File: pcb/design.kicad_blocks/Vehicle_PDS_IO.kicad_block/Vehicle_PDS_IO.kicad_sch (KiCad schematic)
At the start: 1 part, among them J4 FFC2B28-24-G

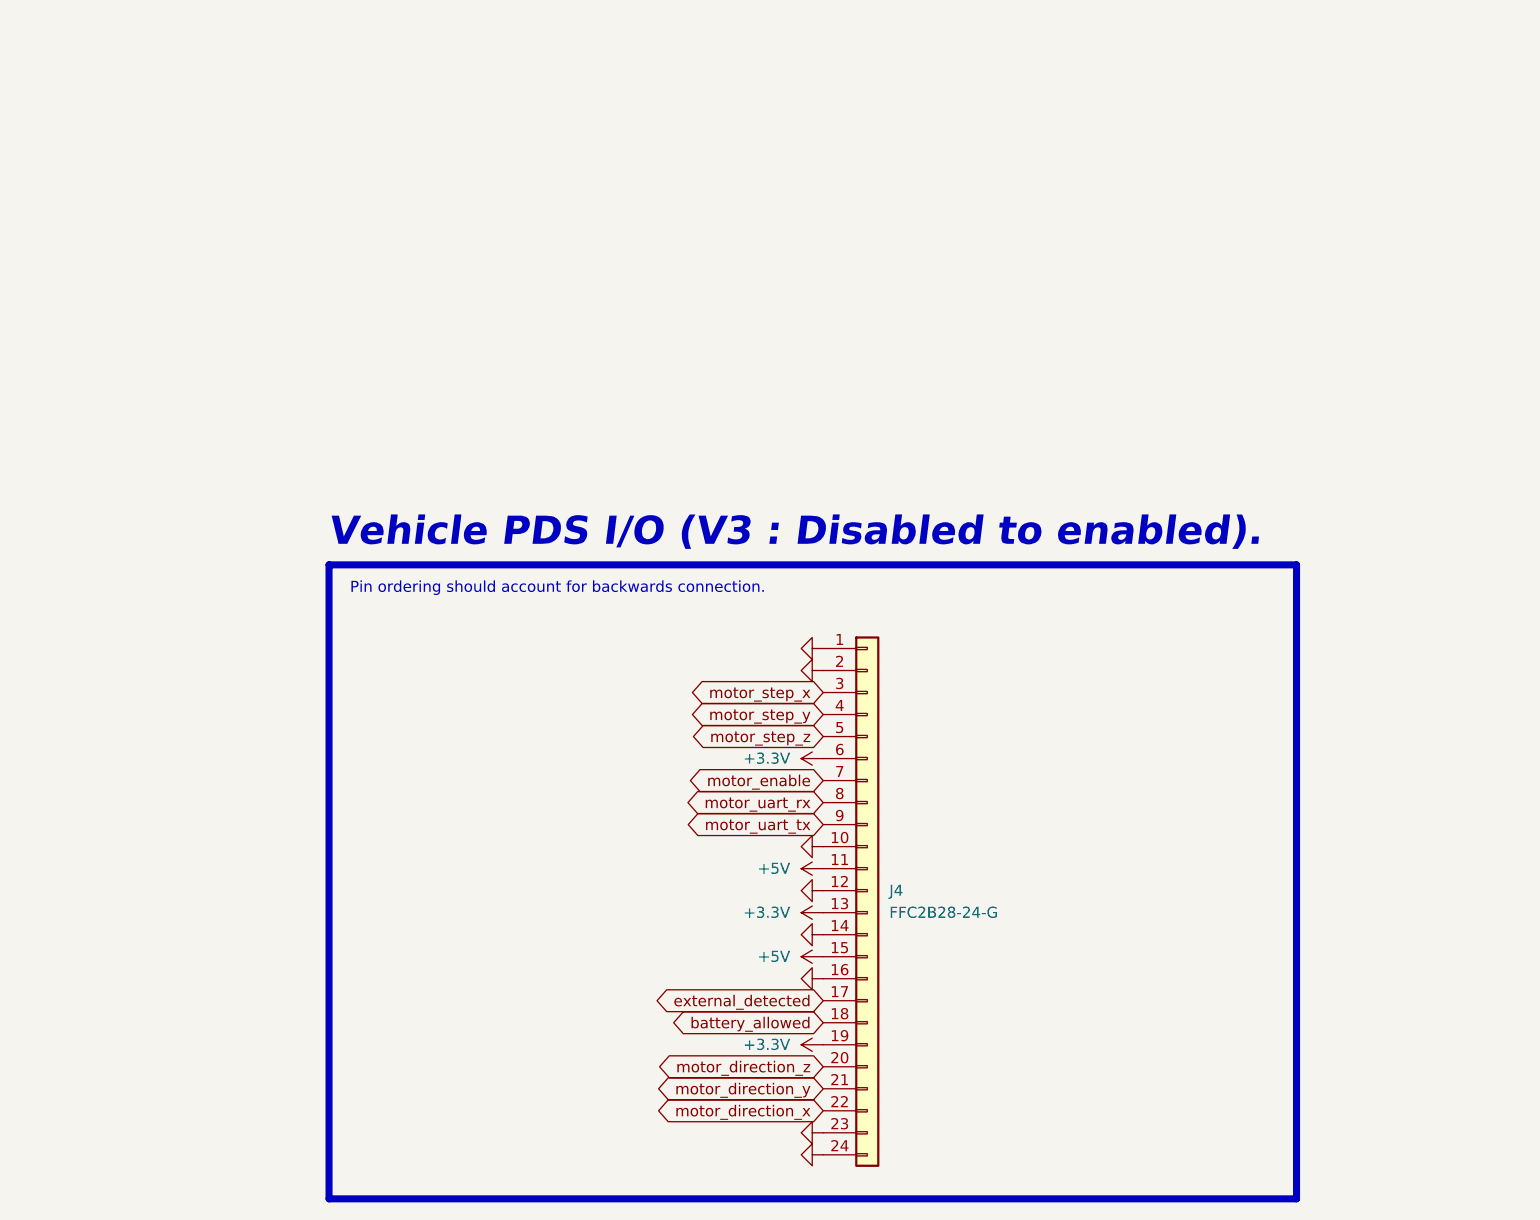
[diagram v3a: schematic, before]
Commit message: Addressed ERC schematic issues for `VehicleFlightComputer`.
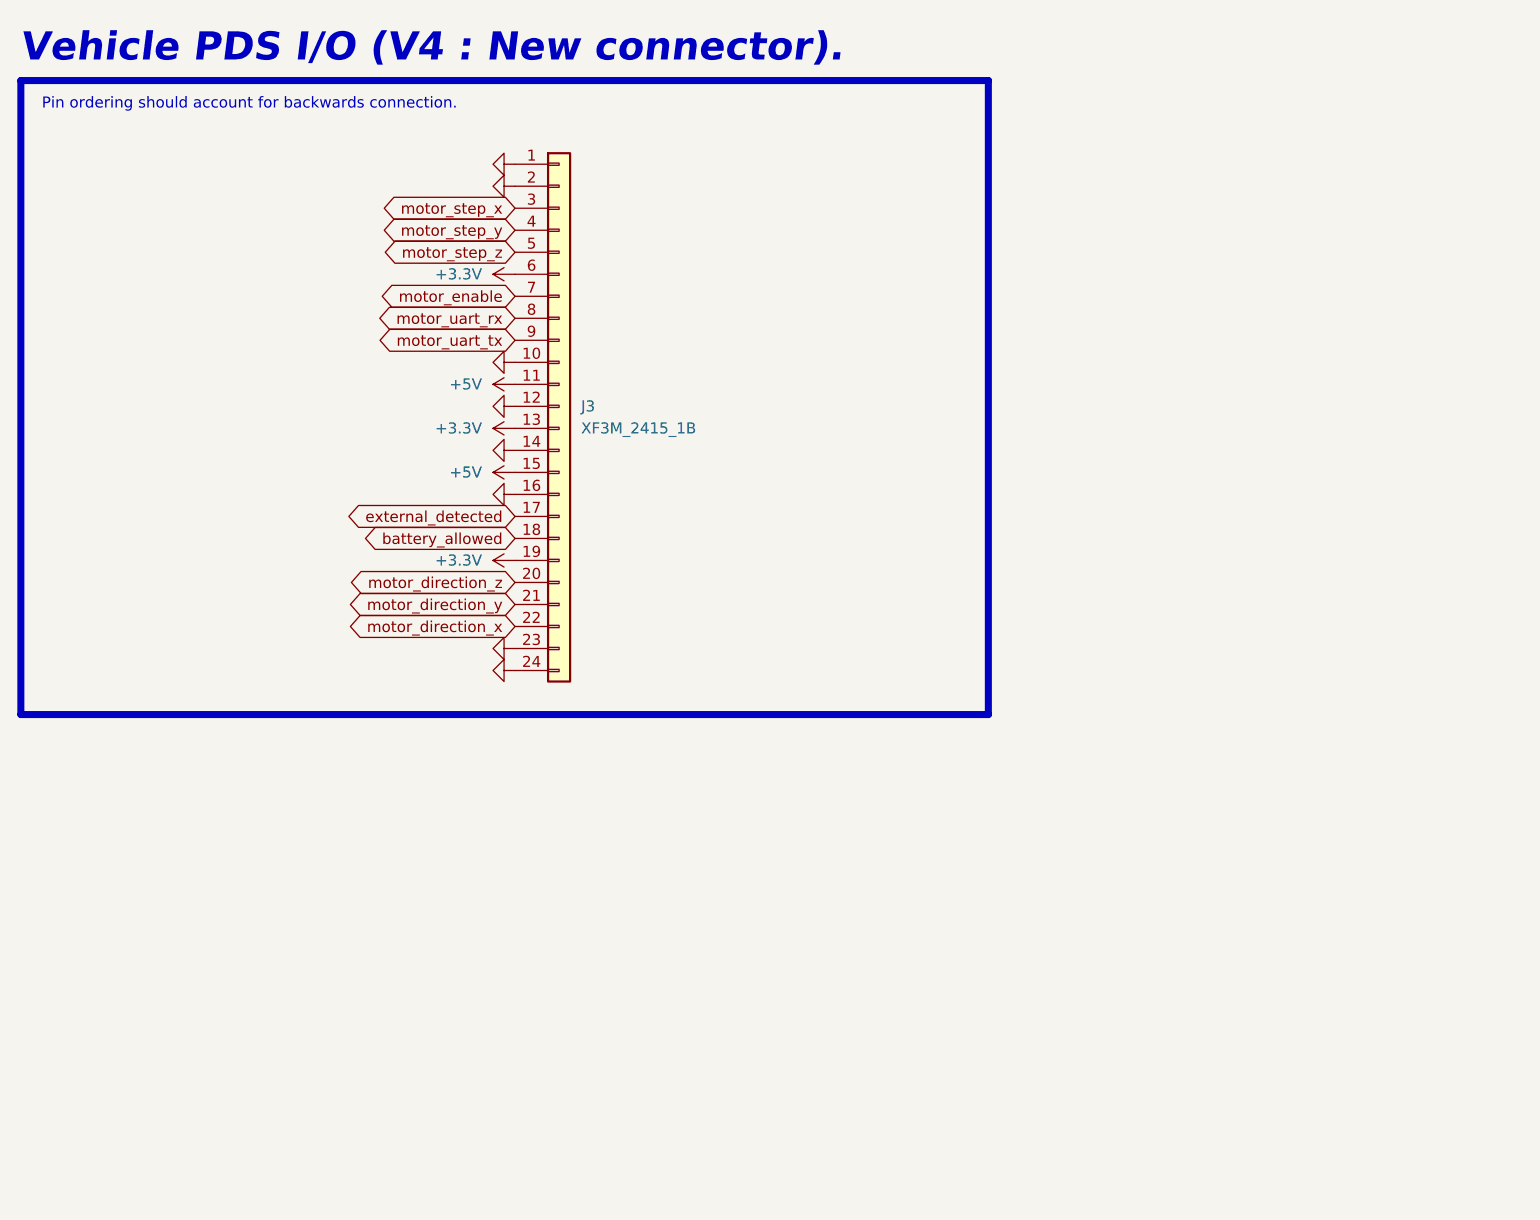
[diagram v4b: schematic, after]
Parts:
- J3: renamed from J4; value FFC2B28-24-G -> XF3M_2415_1B; footprint pcb:Flat Flexible Cable 24-Pin 0.5mm Connector -> pcb:XF3M_2415_1B
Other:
- note added: "Vehicle PDS I/O (V4 : New connector)."
- note removed: "Vehicle PDS I/O (V3 : Disabled to enabled)."
- moved on the sheet: J3

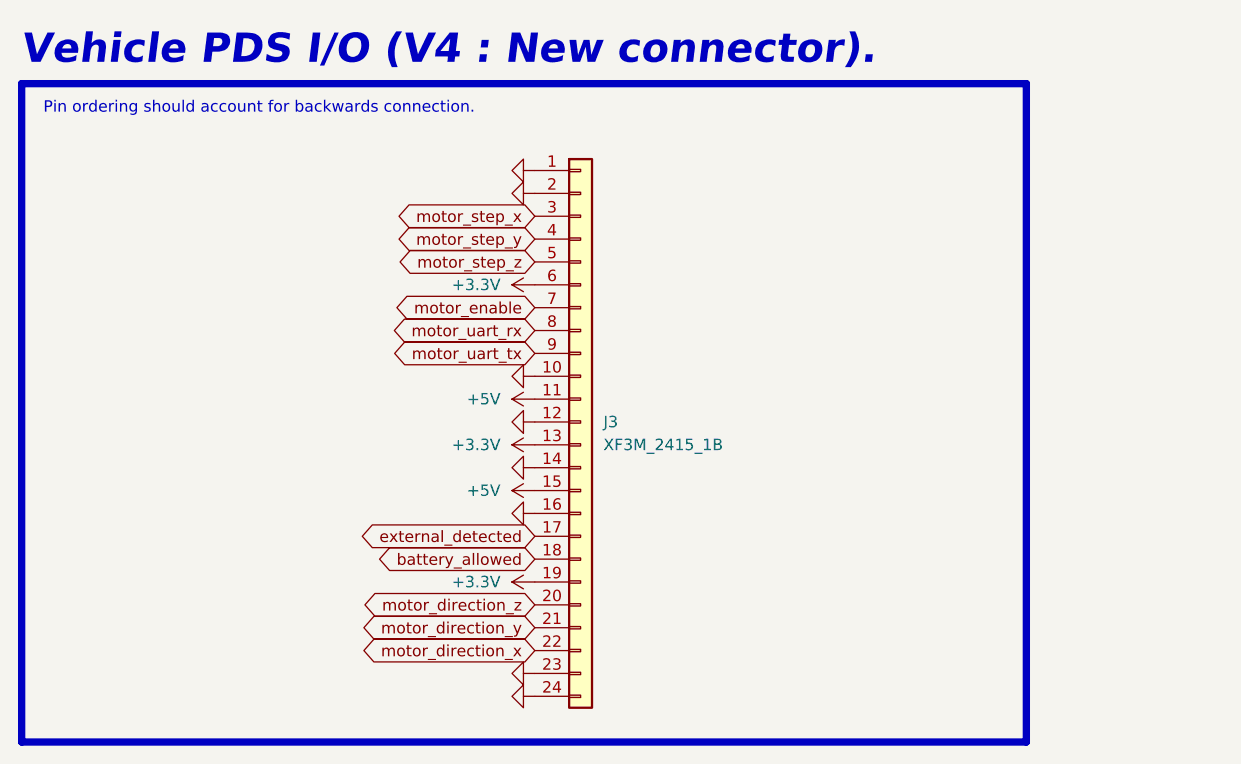
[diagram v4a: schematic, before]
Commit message: Deprecated `motor_uart_rx` for `VehicleFlightComputer` and `VehiclePowerDistributionSystem`.
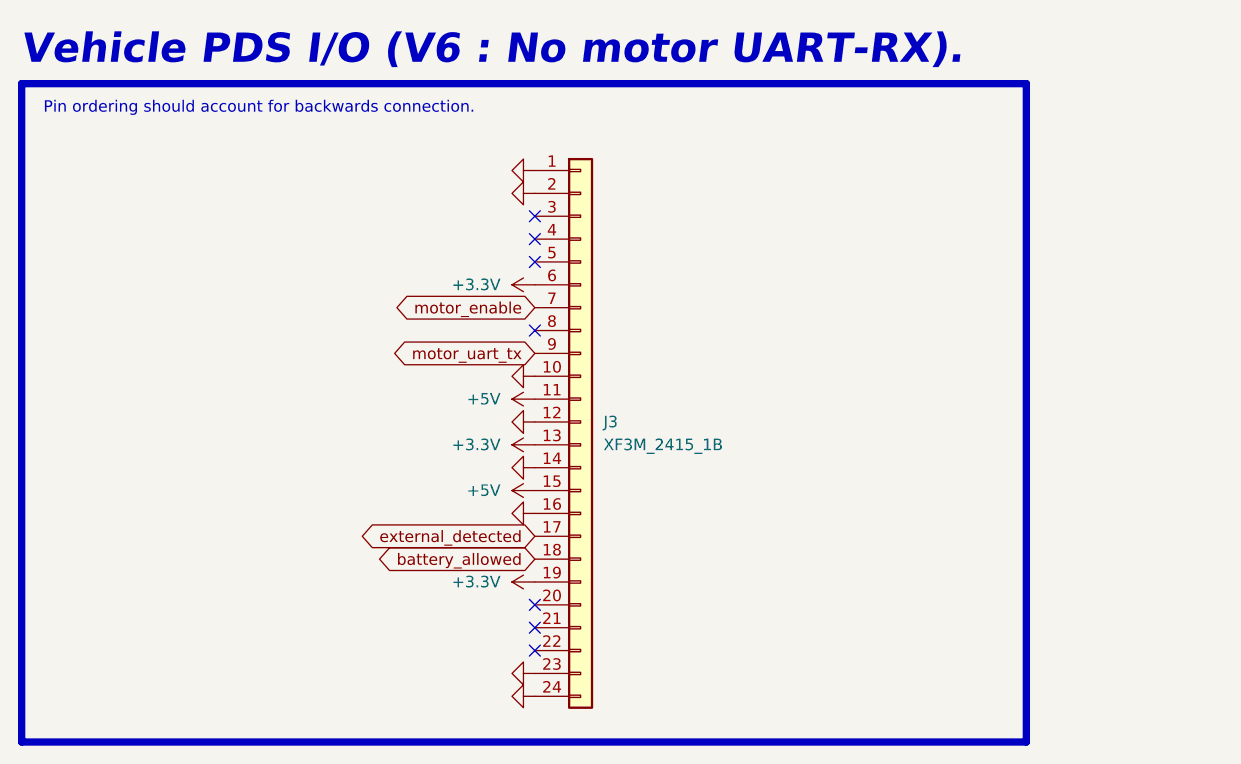
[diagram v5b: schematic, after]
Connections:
- net motor_direction_x: no longer names the net of J3.22 (Pin_22)
- net motor_direction_y: no longer names the net of J3.21 (Pin_21)
- net motor_direction_z: no longer names the net of J3.20 (Pin_20)
- net motor_step_x: no longer names the net of J3.3 (Pin_3)
- net motor_step_y: no longer names the net of J3.4 (Pin_4)
- net motor_step_z: no longer names the net of J3.5 (Pin_5)
- net motor_uart_rx: no longer names the net of J3.8 (Pin_8)
- no-connect marks 0 -> 7
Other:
- note added: "Vehicle PDS I/O (V6 : No motor UART-RX)."
- note removed: "Vehicle PDS I/O (V4 : New connector)."
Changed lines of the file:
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@@
 		)
 	)
-	(text "Vehicle PDS I/O (V4 : New connector)."
+	(text "Vehicle PDS I/O (V6 : No motor UART-RX)."
 		(exclude_from_sim no)
 		(at 427.99 241.3 0)
@@
 		)
 	)
-	(global_label "motor_direction_x"
-		(shape bidirectional)
-		(at 485.14 306.07 180)
-		(fields_autoplaced yes)
-		(effects
-			(font
-				(size 1.27 1.27)
-			)
-			(justify right)
-		)
-		(property "Intersheetrefs" "${INTERSHEET_REFS}"
-			(at 464.2313 306.07 0)
-			(effects
-				(font
-					(size 1.27 1.27)
-				)
-				(justify right)
-				(hide yes)
-			)
-		)
+	(no_connect
+		(at 485.14 262.89)
+	)
+	(no_connect
+		(at 485.14 270.51)
+	)
+	(no_connect
+		(at 485.14 303.53)
+	)
+	(no_connect
+		(at 485.14 260.35)
+	)
+	(no_connect
+		(at 485.14 300.99)
+	)
+	(no_connect
+		(at 485.14 306.07)
+	)
+	(no_connect
+		(at 485.14 257.81)
 	)
 	(global_label "external_detected"
@@
 		(property "Intersheetrefs" "${INTERSHEET_REFS}"
 			(at 466.2876 295.91 0)
-			(effects
-				(font
-					(size 1.27 1.27)
-				)
-				(justify right)
-				(hide yes)
-			)
-		)
-	)
-	(global_label "motor_direction_y"
-		(shape bidirectional)
-		(at 485.14 303.53 180)
-		(fields_autoplaced yes)
-		(effects
-			(font
-				(size 1.27 1.27)
-			)
-			(justify right)
-		)
-		(property "Intersheetrefs" "${INTERSHEET_REFS}"
-			(at 464.2918 303.53 0)
-			(effects
-				(font
-					(size 1.27 1.27)
-				)
-				(justify right)
-				(hide yes)
-			)
-		)
-	)
-	(global_label "motor_step_x"
-		(shape bidirectional)
-		(at 485.14 257.81 180)
-		(fields_autoplaced yes)
-		(effects
-			(font
-				(size 1.27 1.27)
-			)
-			(justify right)
-		)
-		(property "Intersheetrefs" "${INTERSHEET_REFS}"
-			(at 468.5856 257.81 0)
 			(effects
 				(font
@@
 			(effects
 				(font
-					(size 1.27 1.27)
-				)
-				(justify right)
-				(hide yes)
-			)
-		)
-	)
-	(global_label "motor_direction_z"
-		(shape bidirectional)
-		(at 485.14 300.99 180)
-		(fields_autoplaced yes)
-		(effects
-			(font
-				(size 1.27 1.27)
-			)
-			(justify right)
-		)
-		(property "Intersheetrefs" "${INTERSHEET_REFS}"
-			(at 464.2313 300.99 0)
-			(effects
-				(font
-					(size 1.27 1.27)
-				)
-				(justify right)
-				(hide yes)
-			)
-		)
-	)
-	(global_label "motor_step_y"
-		(shape bidirectional)
-		(at 485.14 260.35 180)
-		(fields_autoplaced yes)
-		(effects
-			(font
-				(size 1.27 1.27)
-			)
-			(justify right)
-		)
-		(property "Intersheetrefs" "${INTERSHEET_REFS}"
-			(at 468.6461 260.35 0)
-			(effects
-				(font
-					(size 1.27 1.27)
-				)
-				(justify right)
-				(hide yes)
-			)
-		)
-	)
-	(global_label "motor_uart_rx"
-		(shape bidirectional)
-		(at 485.14 270.51 180)
-		(fields_autoplaced yes)
-		(effects
-			(font
-				(size 1.27 1.27)
-			)
-			(justify right)
-		)
-		(property "Intersheetrefs" "${INTERSHEET_REFS}"
-			(at 467.9809 270.51 0)
-			(effects
-				(font
-					(size 1.27 1.27)
-				)
-				(justify right)
-				(hide yes)
-			)
-		)
-	)
-	(global_label "motor_step_z"
-		(shape bidirectional)
-		(at 485.14 262.89 180)
-		(fields_autoplaced yes)
-		(effects
-			(font
-				(size 1.27 1.27)
-			)
-			(justify right)
-		)
-		(property "Intersheetrefs" "${INTERSHEET_REFS}"
-			(at 468.5856 262.89 0)
-			(effects
-				(font

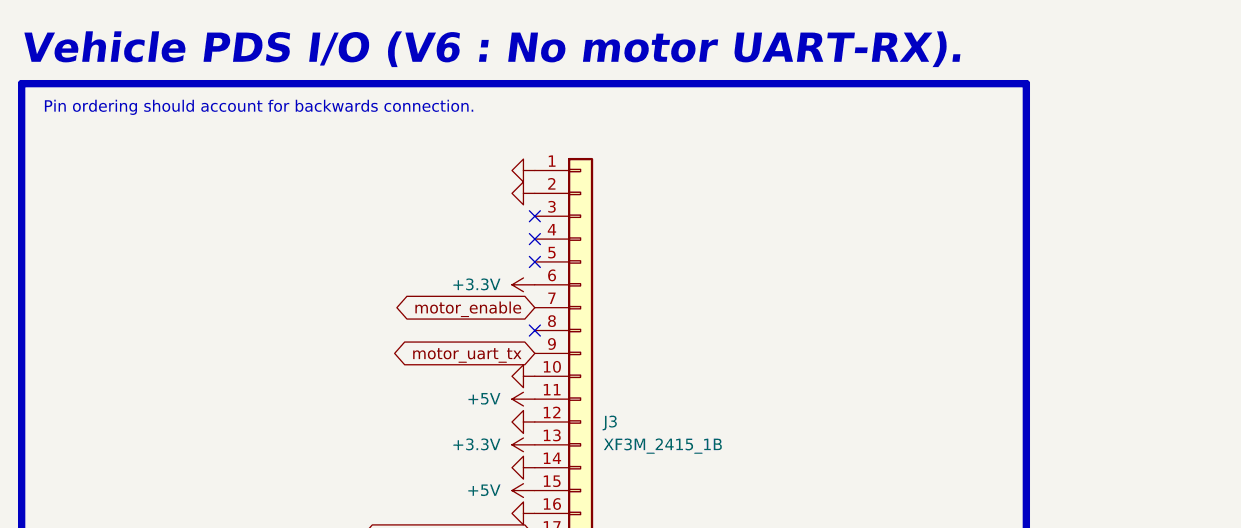
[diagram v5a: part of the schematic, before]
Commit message: Updated MCU pin-outs for `VehicleFlightComputer`.
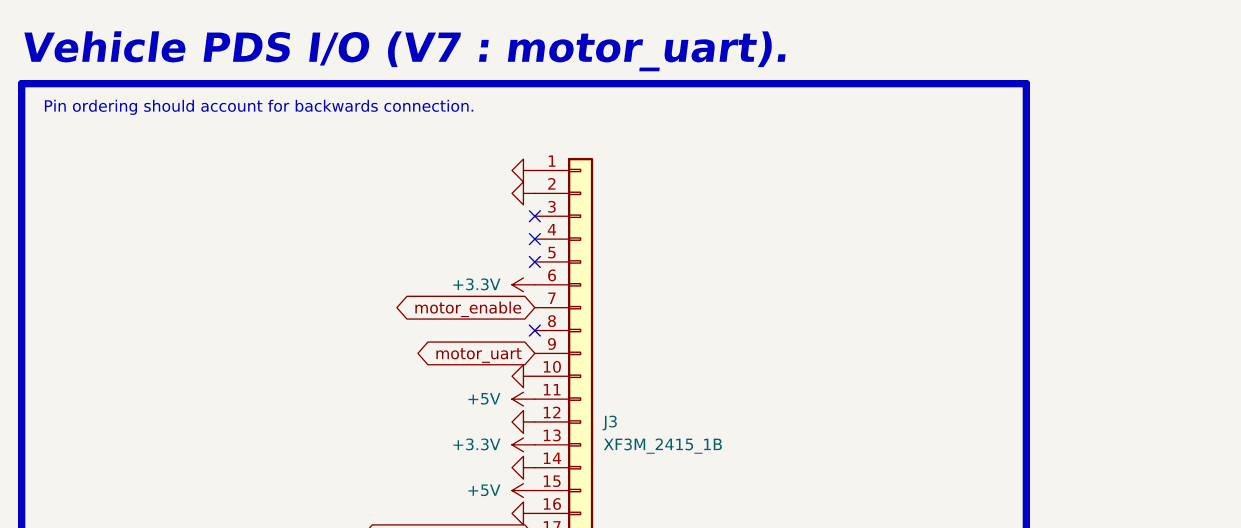
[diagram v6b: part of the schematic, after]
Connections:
- net motor_uart_tx renamed motor_uart
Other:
- note added: "Vehicle PDS I/O (V7 : motor_uart)."
- note removed: "Vehicle PDS I/O (V6 : No motor UART-RX)."
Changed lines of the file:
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@@
 		)
 	)
-	(text "Vehicle PDS I/O (V6 : No motor UART-RX)."
+	(text "Vehicle PDS I/O (V7 : motor_uart)."
 		(exclude_from_sim no)
 		(at 427.99 241.3 0)
@@
 		)
 	)
-	(global_label "motor_uart_tx"
+	(global_label "motor_uart"
 		(shape bidirectional)
 		(at 485.14 273.05 180)
@@
 		)
 		(property "Intersheetrefs" "${INTERSHEET_REFS}"
-			(at 468.0414 273.05 0)
+			(at 470.7628 273.05 0)
 			(effects
 				(font

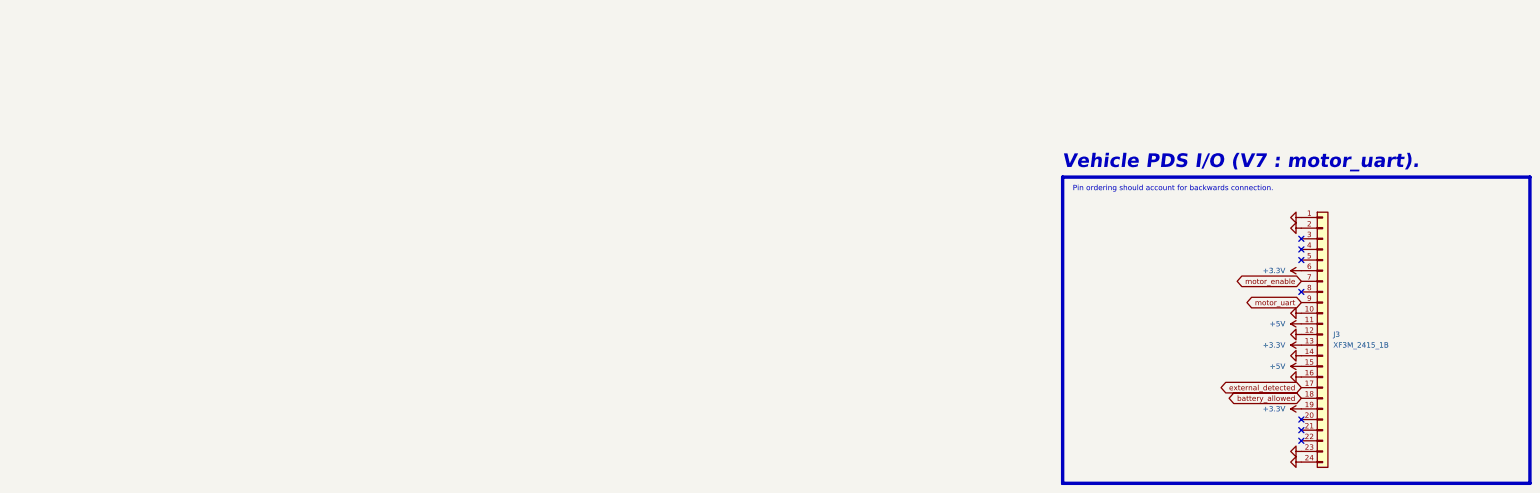
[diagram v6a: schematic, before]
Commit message: Revised `VehiclePowerDistributionSystem`.
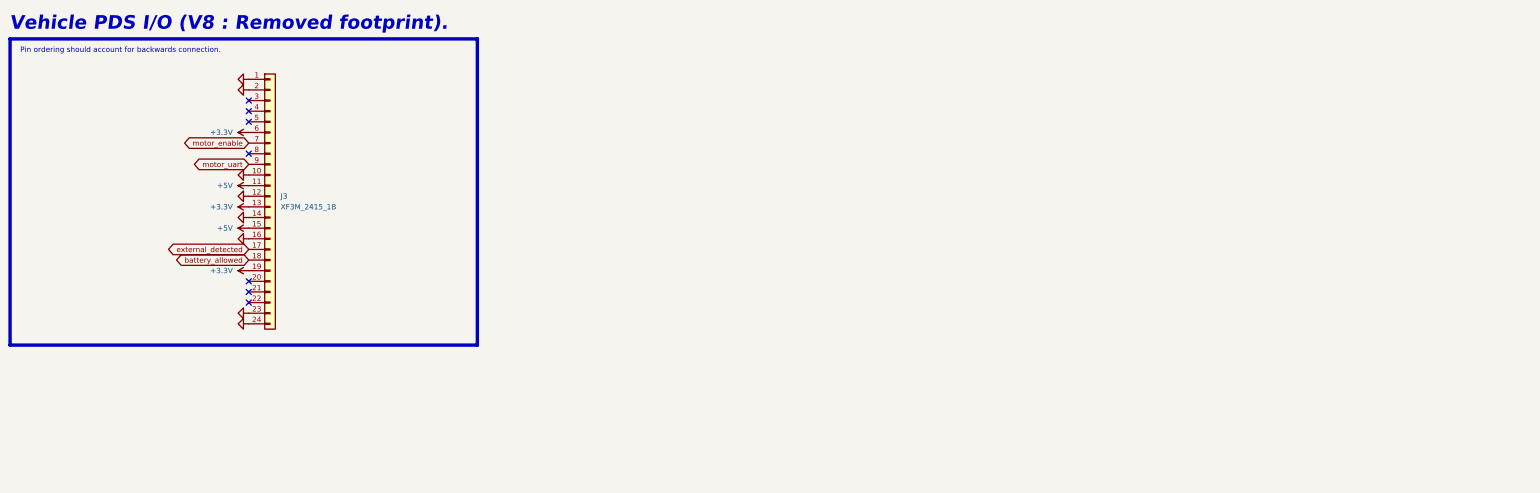
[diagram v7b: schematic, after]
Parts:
- J3: footprint pcb:XF3M_2415_1B -> (none)
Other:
- note added: "Vehicle PDS I/O (V8 : Removed footprint)."
- note removed: "Vehicle PDS I/O (V7 : motor_uart)."
- moved on the sheet: J3
